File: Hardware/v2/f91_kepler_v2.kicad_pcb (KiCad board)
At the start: 2 copper layers, 25 x 27 mm, 89 parts, among them J1 LS013B7DH03 FPC, Q1 FS8205A, SW1 BTN1/BSL, SW2 BTN2, SW3 BTN3, U1 CC2652R7RGZ, U2 BQ51050B, U3 DW01A, U4 XC6206P302MR, U5 LIS2DW12, U6 DRV2605L, U7 ST25DV04K, Y1 48MHz FA-128, Y2 32.768kHz FC-135

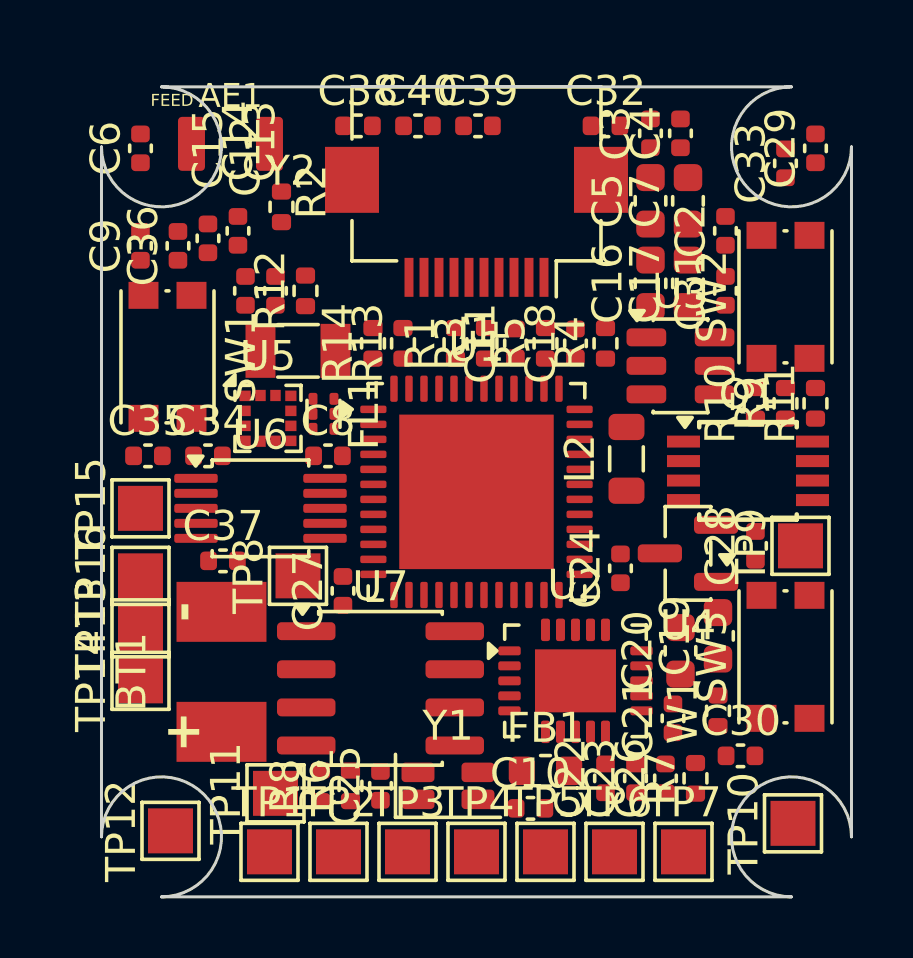
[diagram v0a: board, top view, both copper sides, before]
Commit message: feat(hw/v2): route RF chain + power plane, fix XTAL/balun/VDDR placement
- Y1 48MHz XTAL: bottom edge (13mm from U1) -> (10.70,8.55) beside pins 46/47
- FL1 balun rot270->rot180: RF_P direct on F.Cu, no crossover
- C8 VDDR cap -> (16.40,9.90) beside L2; frees FL1 south escape pocket
- netclasses RF (0.25/0.15) + POWER (0.35); .kicad_dru rf_relax + U5/FL1
  land-pattern pad exceptions
- hand-routed locked: RF_P, X48M_P/N, ANT_FEED, RF_N (via-in-pad 0.4/0.2
  at U1.2), RF_UNBAL (B.Cu sweep to match network)
- GND pours F+B (solid connect), stitching vias, freerouting 1.9 session
  imported (~80 nets); board min drill 0.2 / via 0.4
- DRC: 0 real violations (1 documented corner-arc phantom on ANT_FEED)
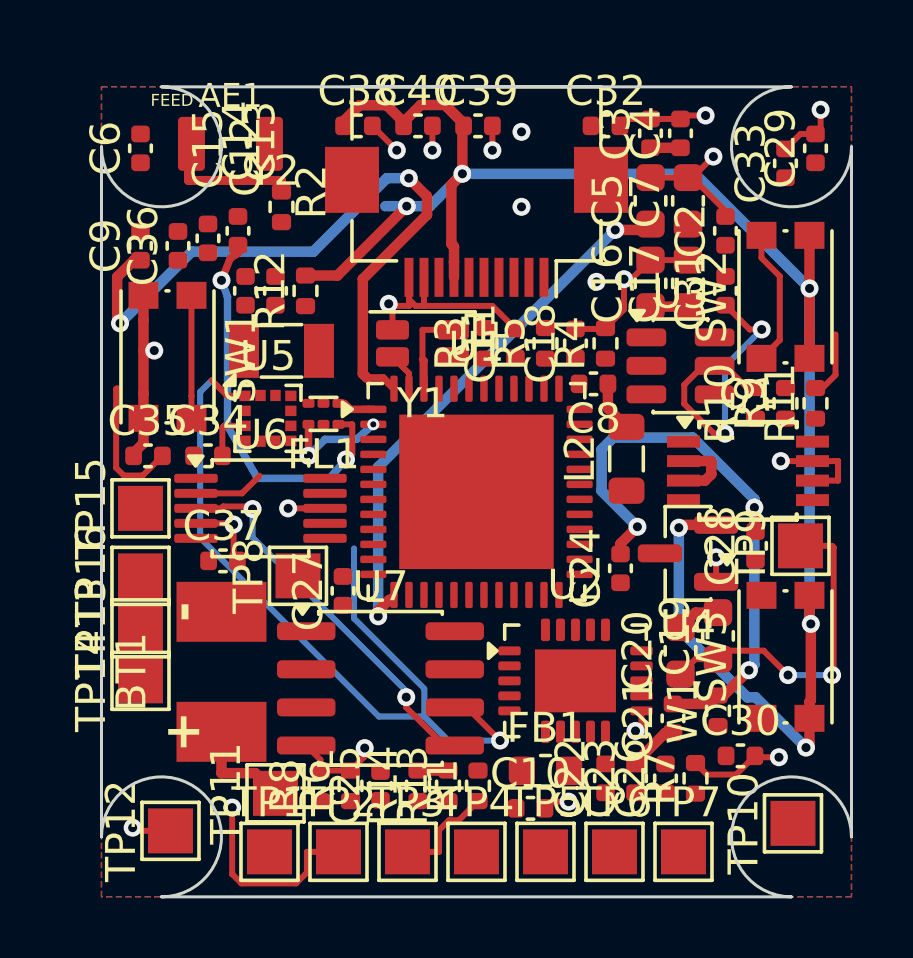
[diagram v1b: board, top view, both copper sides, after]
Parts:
- moved R13 14.8 mm to (11.6, 23.3)
- moved R14 14.8 mm to (10.6, 23.3)
- moved Y1 14.8 mm to (10.7, 8.55), turned to 180 degrees
- moved R1 14.8 mm to (12.6, 23.3)
- moved C8 9.17 mm to (16.4, 9.90), turned to 180 degrees
- moved Y2 0.55 mm to (6.00, 8.80)
- turned FL1 to 180 degrees
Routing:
- net +3V0: track 0.00 -> 69.6 mm, vias 0 -> 7
- net GND: track 0.00 -> 57.0 mm, vias 0 -> 21
- net SCL: track 0.00 -> 30.4 mm, vias 0 -> 1
- net VDDR: track 0.00 -> 24.8 mm, vias 0 -> 2
- net AC2: track 0.00 -> 19.9 mm, vias 0 -> 3
- net VDDS: track 0.00 -> 19.3 mm, vias 0 -> 2
- net SDA: track 0.00 -> 12.8 mm, vias 0 -> 2
- net RF_UNBAL: track 0.00 -> 12.8 mm, vias 0 -> 2
- net COIL1: track 0.00 -> 11.1 mm, vias 0 -> 2
- net DW_VCC: track 0.00 -> 10.9 mm, vias 0 -> 2
- net BTN_2: track 0.00 -> 4.60 mm
- net BTN_1: track 0.00 -> 4.10 mm
- net X48M_N: track 0.00 -> 3.96 mm
- net ANT_FEED: track 0.00 -> 3.80 mm
- net RF_N: track 0.00 -> 3.48 mm, vias 0 -> 2
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- added copper zone on B.Cu, net GND
- added copper zone on F.Cu, net GND

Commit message: feat(hw/v2): route 70% of board — freerouting + custom A* grid router
- freerouting 1.9 (3 rounds; 2.1 has maze crash) + custom SES importer
  (ImportSpecctraSES segfaults on 1.9 sessions)
- tools/grid_router.py: A* on 0.05mm grid, per-net dilated obstacle
  masks, no corner cutting, via-disc feasibility, GND/POWER/signal
  ordering; exact rect rounding preserves fine-pitch pin escapes
- 198 -> 90 unconnected; DRC clean (1 documented corner-arc phantom)
- remaining nets blocked by placement: U1-U2 gap 0.35mm traps U1 south
  pads (LCD/BTN_1/SWD), Qi charger cluster walls PROT_*/CHG_DET/ILIM
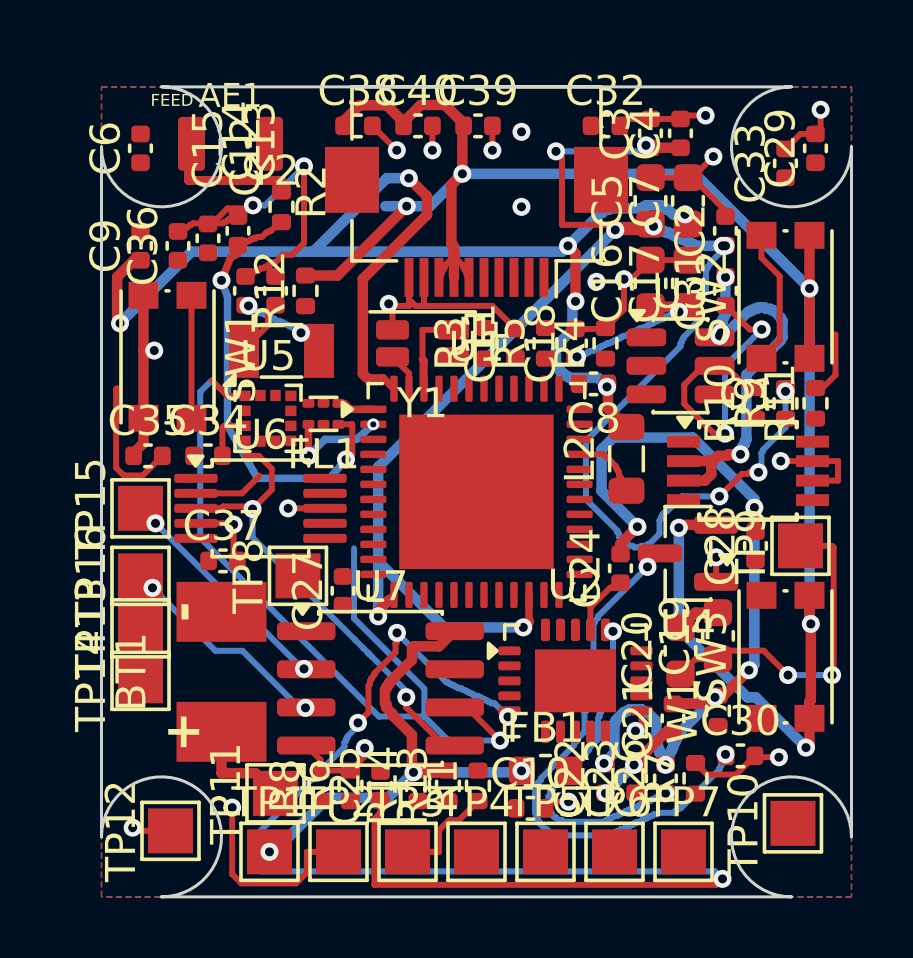
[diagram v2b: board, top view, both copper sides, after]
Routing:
- net CLAMP1: track 0.00 -> 45.3 mm, vias 0 -> 4
- net VDDS: track 19.3 -> 59.4 mm, vias 2 -> 11
- net +3V0: track 69.6 -> 91.7 mm, vias 7 -> 10
- net VDDR: track 24.8 -> 44.9 mm, vias 2 -> 6
- net VBAT: track 3.46 -> 22.0 mm, vias 0 -> 2
- net CLAMP2: track 0.00 -> 11.6 mm, vias 0 -> 2
- net BATN: track 2.38 -> 13.7 mm, vias 0 -> 4
- net GND: track 57.0 -> 68.2 mm, vias 21 -> 23
- net AC2: track 19.9 -> 29.3 mm, vias 3 -> 6
- net NFC_A: track 0.00 -> 7.75 mm, vias 0 -> 2
- net NFC_B: track 0.00 -> 7.35 mm, vias 0 -> 2
- net RECT: track 1.25 -> 5.79 mm, vias 0 -> 2
- net SDA: track 12.8 -> 16.0 mm
- net X32K_1: track 0.00 -> 3.10 mm, vias 0 -> 2
- net DCDC_SW: track 0.00 -> 2.31 mm
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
